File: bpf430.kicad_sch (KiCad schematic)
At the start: 39 parts

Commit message: 部品定数を入力　ただし未評価
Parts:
- C403, C405, C407, C409, C411, C413, C415, C417, C419, C421, C423, C425, C427: value 1p -> NM
- C404, C428: value 10p -> 12p
- C410, C426: value 10p -> 15p
- C418: value 10p -> 5p
- L403, L405: value 10n -> NM
- L404, L406: value 1u -> 3.3n
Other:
- note added: "1t D3.5mm L2.0mm"
- note added: "Butterworth 410M-460M 6.68p, 3.32p, 34.0p"
- company: (none) -> JK1MLY / PRUG
- title: (none) -> FM QRP TRCV

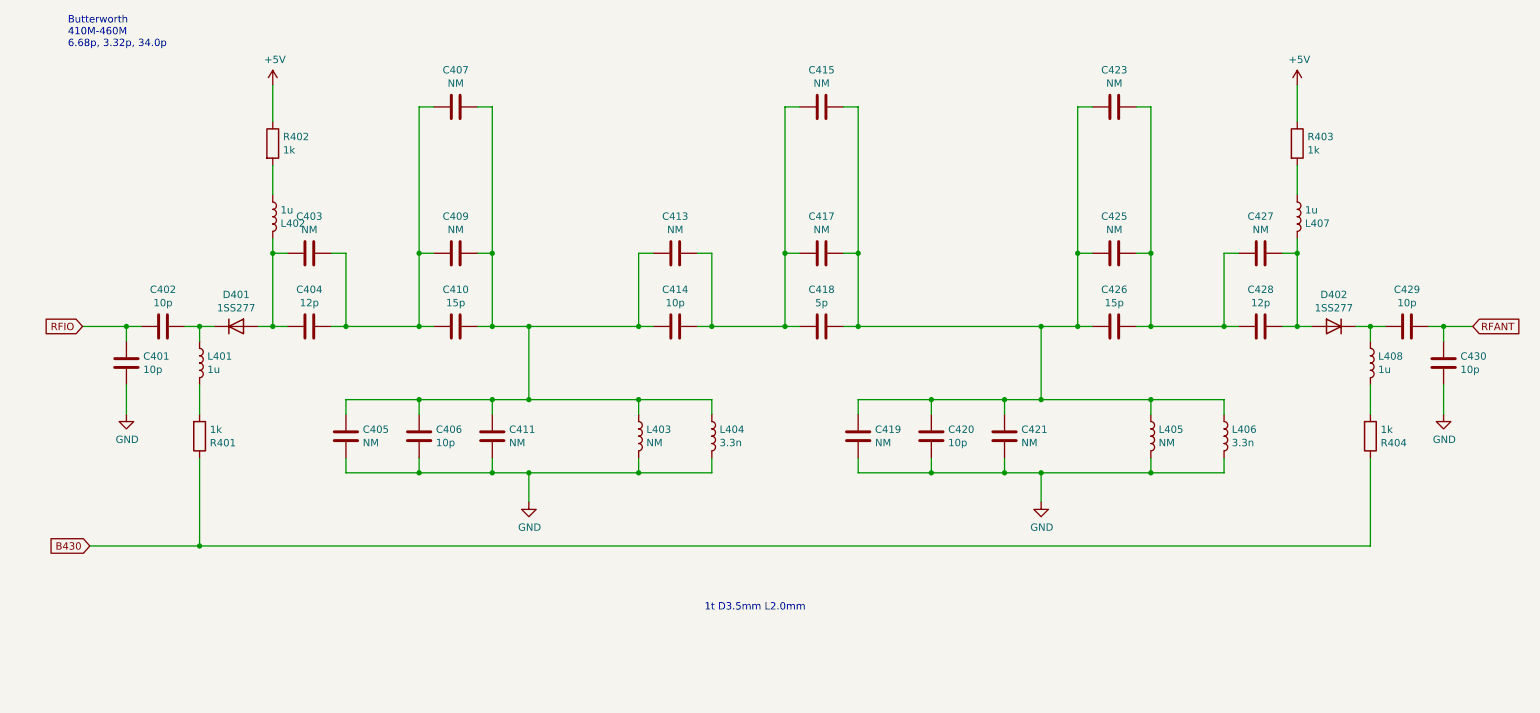
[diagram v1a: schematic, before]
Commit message: バンドパスフィルタの定数を見直し（単体試験の反映）
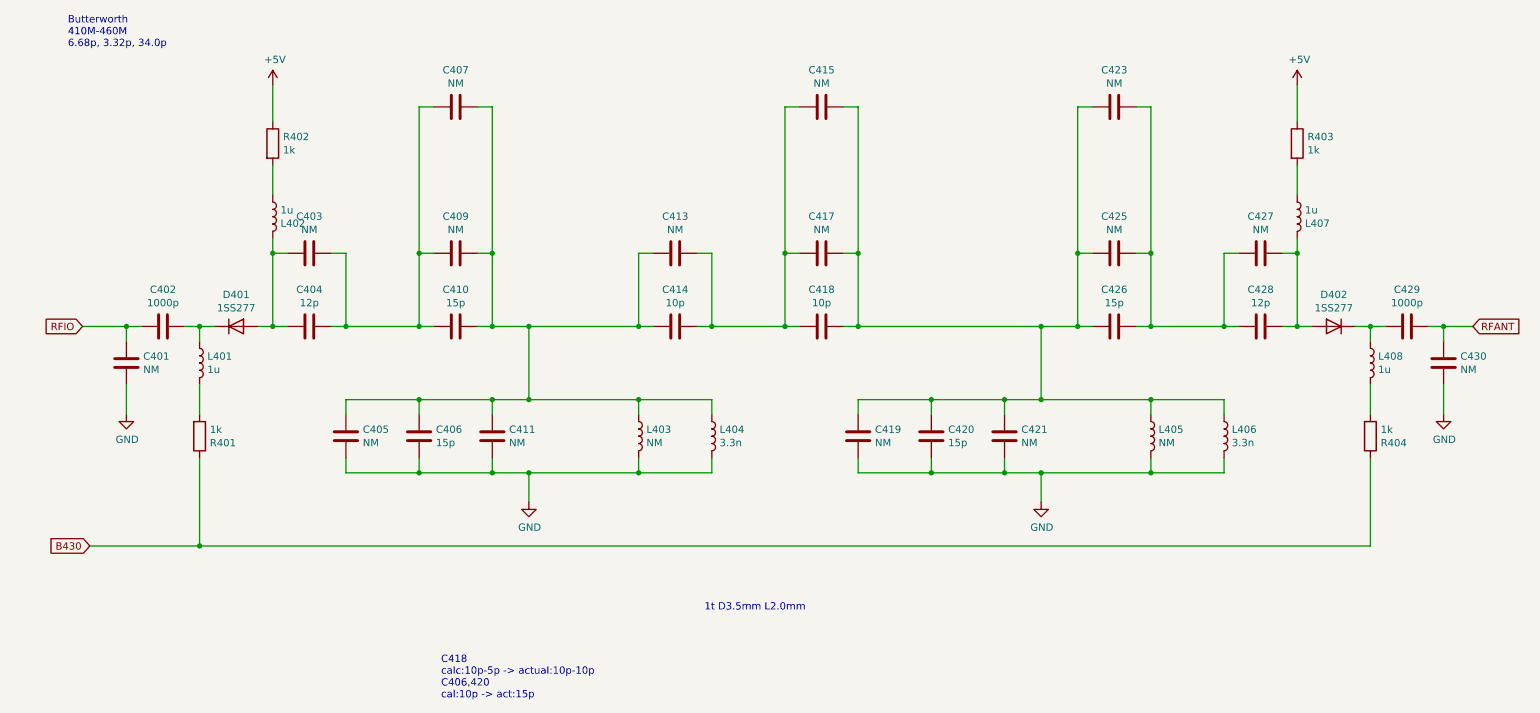
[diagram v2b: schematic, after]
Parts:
- C401, C430: value 10p -> NM
- C402, C429: value 10p -> 1000p
- C406, C420: value 10p -> 15p
- C418: value 5p -> 10p
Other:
- note added: "C418 calc:10p-5p -> actual:10p-10p C406,420 cal:10p -> act:15p"
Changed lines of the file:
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@@
+    (effects (font (size 1.27 1.27)) (justify left bottom))
+  )
+  (text "C418\ncalc:10p-5p -> actual:10p-10p\nC406,420\ncal:10p -> act:15p"
+    (at 92.71 140.97 0)
     (effects (font (size 1.27 1.27)) (justify left bottom))
   )
@@
       (effects (font (size 1.27 1.27)) (justify left))
     )
-    (property "Value" "10p" (id 1) (at 180.721 96.393 0)
+    (property "Value" "15p" (id 1) (at 180.721 96.393 0)
       (effects (font (size 1.27 1.27)) (justify left))
     )
@@
     (in_bom yes) (on_board yes)
     (property "Reference" "C418" (id 0) (at 158.75 69.7992 90))
-    (property "Value" "5p" (id 1) (at 158.75 72.1106 90))
+    (property "Value" "10p" (id 1) (at 158.75 72.1106 90))
     (property "Footprint" "Capacitor_THT:C_Disc_D3.4mm_W2.1mm_P2.50mm" (id 2) (at 162.56 75.2348 0)
       (effects (font (size 1.27 1.27)) hide)
@@
       (effects (font (size 1.27 1.27)) (justify left))
     )
-    (property "Value" "10p" (id 1) (at 91.821 96.393 0)
+    (property "Value" "15p" (id 1) (at 91.821 96.393 0)
       (effects (font (size 1.27 1.27)) (justify left))
     )
@@
     (in_bom yes) (on_board yes)
     (property "Reference" "C429" (id 0) (at 260.35 69.7992 90))
-    (property "Value" "10p" (id 1) (at 260.35 72.1106 90))
+    (property "Value" "1000p" (id 1) (at 260.35 72.1106 90))
     (property "Footprint" "Capacitor_THT:C_Disc_D3.4mm_W2.1mm_P2.50mm" (id 2) (at 264.16 75.2348 0)
       (effects (font (size 1.27 1.27)) hide)
@@
     (in_bom yes) (on_board yes)
     (property "Reference" "C402" (id 0) (at 44.45 69.7992 90))
-    (property "Value" "10p" (id 1) (at 44.45 72.1106 90))
+    (property "Value" "1000p" (id 1) (at 44.45 72.1106 90))
     (property "Footprint" "Capacitor_THT:C_Disc_D3.4mm_W2.1mm_P2.50mm" (id 2) (at 48.26 75.2348 0)
       (effects (font (size 1.27 1.27)) hide)
@@
       (effects (font (size 1.27 1.27)) (justify left))
     )
-    (property "Value" "10p" (id 1) (at 41.021 83.693 0)
+    (property "Value" "NM" (id 1) (at 41.021 83.693 0)
       (effects (font (size 1.27 1.27)) (justify left))
     )
@@
       (effects (font (size 1.27 1.27)) (justify left))
     )
-    (property "Value" "10p" (id 1) (at 269.621 83.693 0)
-      (effects (font (size 1.27 1.27)) (justify left))
-    )
+    (property "Value" "NM" (id 1) (at 269.621 83.693 0)
+      (effects (font (size 1.27 1.27)) (justify left))
+    )

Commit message: Add files via upload
フィルタ回路変更とジャンパクリーン
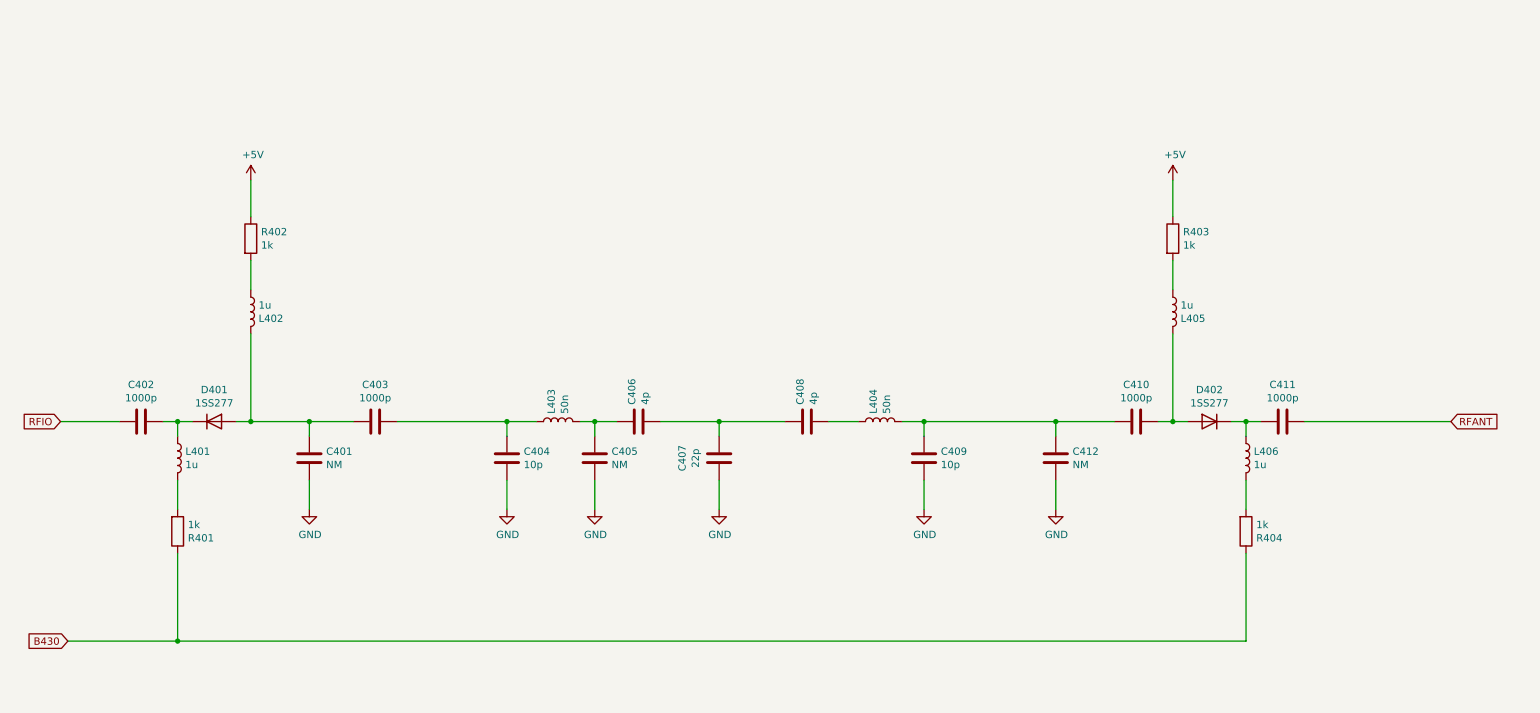
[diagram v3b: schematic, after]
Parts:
- removed C403, C411, C413, C415, C417, C419, C421, C423, C425, C427: NM, digikey-footprints:0603, symbol Device:C
- removed C410, C420, C426: 15p, Capacitor_THT:C_Disc_D3.4mm_W2.1mm_P2.50mm, symbol Device:C
- removed C414, C418: 10p, Capacitor_THT:C_Disc_D3.4mm_W2.1mm_P2.50mm, symbol Device:C
- removed L405: NM, Inductor_SMD:L_Murata_LQH2MCNxxxx02_2.0x1.6mm, symbol Device:L
- removed L406: 3.3n, Resistor_THT:R_Axial_DIN0204_L3.6mm_D1.6mm_P5.08mm_Horizontal, symbol Device:L
- added C404: 10p, Capacitor_THT:C_Disc_D3.4mm_W2.1mm_P2.50mm, symbol Device:C
- added C408: 4p, Capacitor_THT:C_Disc_D3.4mm_W2.1mm_P2.50mm, symbol Device:C
- C403: renamed from C404; value 12p -> 1000p
- C405: footprint digikey-footprints:0603 -> Capacitor_THT:C_Disc_D3.4mm_W2.1mm_P2.50mm
- C406: value 15p -> 4p
- C407: value NM -> 22p; footprint digikey-footprints:0603 -> Capacitor_THT:C_Disc_D3.4mm_W2.1mm_P2.50mm
- C409: value NM -> 10p; footprint digikey-footprints:0603 -> Capacitor_THT:C_Disc_D3.4mm_W2.1mm_P2.50mm
- C410: renamed from C428; value 12p -> 1000p
- L403: value NM -> 50n; footprint Inductor_SMD:L_Murata_LQH2MCNxxxx02_2.0x1.6mm -> usr-Library:coil3_7mm
- L404: value 3.3n -> 50n; footprint Resistor_THT:R_Axial_DIN0204_L3.6mm_D1.6mm_P5.08mm_Horizontal -> usr-Library:coil3_7mm
- renumbered C429 to C411, C430 to C412, L407 to L405, L408 to L406
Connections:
- net GND: now also C407.1, C409.2, C404.2; no longer C406.2, L403.2, L404.2
- net RFANT: no longer C412.1
- net RFIO: no longer C401.1
- net at C403.1, D401.2 (A), L402.1: now also C401.1
- net at C410.1: now also C409.1, C412.1, L404.2
- new net: C403.2, C404.1, L403.1
- new net: C405.1, C406.1, L403.2
- new net: C406.2, C407.2, C408.1
- new net: C408.2, L404.1
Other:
- note removed: "1t D3.5mm L2.0mm"
- note removed: "Butterworth 410M-460M 6.68p, 3.32p, 34.0p"
- note removed: "C418 calc:10p-5p -> actual:10p-10p C406,420 cal:10p -> act:15p"
- moved on the sheet: C401, C402, C403, C410, C411, C412, D401, D402, L401, L402, L405, L406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

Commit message: アップデート
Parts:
- removed C401, C412: NM, Capacitor_THT:C_Disc_D3.4mm_W2.1mm_P2.50mm, symbol Device:C
- removed C408: 4p, Capacitor_THT:C_Disc_D3.4mm_W2.1mm_P2.50mm, symbol Device:C
- added R102: 1k, Resistor_THT:R_Axial_DIN0207_L6.3mm_D2.5mm_P2.54mm_Vertical, symbol Device:R
- D401, D402: footprint Diode_THT:D_A-405_P2.54mm_Vertical_AnodeUp -> Diode_THT:D_T-1_P5.08mm_Horizontal
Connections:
- net +5V: now also R102.1
- net B430: now also R102.2
- net at C406.2, C407.2: now also L404.1
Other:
- note added: "15p"
- note added: "2p"
- note added: "NM"

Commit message: Add files via upload
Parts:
- C402, C403, C410, C411: value 1000p -> 0.01u
- C404, C409: value 10p -> 5p
- C405: value NM -> 3p
- C406: value 4p -> 15p
- C407: value 22p -> 3p
- L401, L402, L405, L406: value 1u -> 10u
- L403, L404: value 50n -> 20n
- R401, R402, R403, R404: value 1k -> 470
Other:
- note added: "L403,404は5mm 1.5T corecraft 164-01A06L相当 コアは抜き去る 以前はaitendoで入手できたが現在は不可"
- note removed: "15p"
- note removed: "2p"
- note removed: "NM"
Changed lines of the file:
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@@
   (title_block
     (title "FM QRP TRCV")
-    (date "2022-03-12")
+    (date "2023-08-12")
     (rev "1")
     (company "JK1MLY / PRUG")
@@
     (stroke (width 0) (type default))
   )
-  (text "2p" (at 144.78 104.14 0)
-    (effects (font (size 1.27 1.27)) (justify left bottom))
-  )
-  (text "15p" (at 124.46 82.55 0)
-    (effects (font (size 1.27 1.27)) (justify left bottom))
-  )
-  (text "NM" (at 180.34 104.14 0)
-    (effects (font (size 1.27 1.27)) (justify left bottom))
-  )
-  (text "2p" (at 123.19 104.14 0)
-    (effects (font (size 1.27 1.27)) (justify left bottom))
-  )
-  (text "NM" (at 107.95 104.14 0)
+  (text "L403,404は5mm 1.5T\ncorecraft 164-01A06L相当\nコアは抜き去る\n以前はaitendoで入手できたが現在は不可"
+    (at 114.3 73.66 0)
     (effects (font (size 1.27 1.27)) (justify left bottom))
   )
@@
       (effects (font (size 1.27 1.27)) (justify left))
     )
-    (property "Value" "1u" (at 233.7562 100.203 0)
+    (property "Value" "10u" (at 233.7562 100.203 0)
       (effects (font (size 1.27 1.27)) (justify left))
     )
@@
       (effects (font (size 1.27 1.27)) (justify left))
     )
-    (property "Value" "1k" (at 61.468 62.103 0)
+    (property "Value" "470" (at 61.468 62.103 0)
       (effects (font (size 1.27 1.27)) (justify left))
     )
@@
       (effects (font (size 1.27 1.27)) hide)
     )
-    (property "Datasheet" "~" (at 59.69 60.96 0)
+    (property "Datasheet" "R-25471" (at 59.69 60.96 0)
       (effects (font (size 1.27 1.27)) hide)
     )
@@
       (effects (font (size 1.27 1.27)) (justify left))
     )
-    (property "Value" "1k" (at 234.188 110.617 0)
+    (property "Value" "470" (at 234.188 110.617 0)
       (effects (font (size 1.27 1.27)) (justify left))
     )
@@
       (effects (font (size 1.27 1.27)) hide)
     )
-    (property "Datasheet" "~" (at 232.41 111.76 0)
+    (property "Datasheet" "R-25471" (at 232.41 111.76 0)
       (effects (font (size 1.27 1.27)) hide)
     )
@@
       (effects (font (size 1.27 1.27)))
     )
-    (property "Value" "1000p" (at 81.28 88.6206 90)
+    (property "Value" "0.01u" (at 81.28 88.6206 90)
       (effects (font (size 1.27 1.27)))
     )
@@
       (effects (font (size 1.27 1.27)) hide)
     )
-    (property "Datasheet" "~" (at 81.28 92.71 0)
+    (property "Datasheet" "sato" (at 81.28 92.71 0)
       (effects (font (size 1.27 1.27)) hide)
     )
@@
       (effects (font (size 1.27 1.27)))
     )
-    (property "Value" "1000p" (at 213.36 88.6206 90)
+    (property "Value" "0.01u" (at 213.36 88.6206 90)
       (effects (font (size 1.27 1.27)))
     )
@@
       (effects (font (size 1.27 1.27)) hide)
     )
-    (property "Datasheet" "~" (at 213.36 92.71 0)
+    (property "Datasheet" "sato" (at 213.36 92.71 0)
       (effects (font (size 1.27 1.27)) hide)
     )
@@
       (effects (font (size 1.27 1.27)) (justify left))
     )
-    (property "Value" "1u" (at 48.3362 100.203 0)
+    (property "Value" "10u" (at 48.3362 100.203 0)
       (effects (font (size 1.27 1.27)) (justify left))
     )
@@
       (effects (font (size 1.27 1.27)) (justify left))
     )
-    (property "Value" "1k" (at 48.768 110.617 0)
+    (property "Value" "470" (at 48.768 110.617 0)
       (effects (font (size 1.27 1.27)) (justify left))
     )
@@
       (effects (font (size 1.27 1.27)) hide)
     )
-    (property "Datasheet" "~" (at 46.99 111.76 0)
+    (property "Datasheet" "R-25471" (at 46.99 111.76 0)
       (effects (font (size 1.27 1.27)) hide)
     )
@@
       (effects (font (size 1.27 1.27)) (justify left))
     )
-    (property "Value" "1u" (at 61.0362 72.517 0)
+    (property "Value" "10u" (at 61.0362 72.517 0)
       (effects (font (size 1.27 1.27)) (justify left))
     )
@@
       (effects (font (size 1.27 1.27)) (justify left))
     )
-    (property "Value" "1k" (at 221.488 62.103 0)
+    (property "Value" "470" (at 221.488 62.103 0)
       (effects (font (size 1.27 1.27)) (justify left))
     )
@@
       (effects (font (size 1.27 1.27)) hide)
     )
-    (property "Datasheet" "~" (at 219.71 60.96 0)
+    (property "Datasheet" "R-25471" (at 219.71 60.96 0)
       (effects (font (size 1.27 1.27)) hide)
     )
@@
       (effects (font (size 1.27 1.27)) (justify left))
     )
-    (property "Value" "1u" (at 221.0562 72.517 0)
+    (property "Value" "10u" (at 221.0562 72.517 0)
       (effects (font (size 1.27 1.27)) (justify left))
     )
@@
       (effects (font (size 1.27 1.27)))
     )
-    (property "Value" "1000p" (at 238.76 88.6206 90)
+    (property "Value" "0.01u" (at 238.76 88.6206 90)
       (effects (font (size 1.27 1.27)))
     )
@@
       (effects (font (size 1.27 1.27)) hide)
     )
-    (property "Datasheet" "~" (at 238.76 92.71 0)
+    (property "Datasheet" "sato" (at 238.76 92.71 0)
       (effects (font (size 1.27 1.27)) hide)
     )
@@
       (effects (font (size 1.27 1.27)))
     )
-    (property "Value" "1000p" (at 40.64 88.6206 90)
+    (property "Value" "0.01u" (at 40.64 88.6206 90)
       (effects (font (size 1.27 1.27)))
     )
@@
       (effects (font (size 1.27 1.27)) hide)
     )
-    (property "Datasheet" "~" (at 40.64 92.71 0)
+    (property "Datasheet" "sato" (at 40.64 92.71 0)
       (effects (font (size 1.27 1.27)) hide)
     )
@@
       (effects (font (size 1.27 1.27)) (justify left))
     )
-    (property "Value" "NM" (at 122.301 100.203 0)
+    (property "Value" "3p" (at 122.301 100.203 0)
       (effects (font (size 1.27 1.27)) (justify left))
     )
@@
       (effects (font (size 1.27 1.27)) hide)
     )
-    (property "Datasheet" "~" (at 119.38 99.06 0)
+    (property "Datasheet" "sato" (at 119.38 99.06 0)
       (effects (font (size 1.27 1.27)) hide)
     )
@@
       (effects (font (size 1.27 1.27)) (justify left))
     )
-    (property "Value" "50n" (at 170.053 91.3638 0)
+    (property "Value" "20n" (at 170.053 91.3638 0)
       (effects (font (size 1.27 1.27)) (justify left))
     )
@@
       (effects (font (size 1.27 1.27)) hide)
     )
-    (property "Datasheet" "digikey 0805CS-3N3EJTS" (at 168.91 92.71 0)
+    (property "Datasheet" "aitendo" (at 168.91 92.71 0)
       (effects (font (size 1.27 1.27)) hide)
     )
@@
       (effects (font (size 1.27 1.27)) hide)
     )
-    (property "Datasheet" "~" (at 36.83 120.65 0)
+    (property "Datasheet" "R-25102" (at 36.83 120.65 0)
       (effects (font (size 1.27 1.27)) hide)
     )
@@
       (effects (font (size 1.27 1.27)) (justify left))
     )
-    (property "Value" "10p" (at 179.451 100.203 0)
+    (property "Value" "5p" (at 179.451 100.203 0)
       (effects (font (size 1.27 1.27)) (justify left))
     )
@@
       (effects (font (size 1.27 1.27)) hide)
     )
-    (property "Datasheet" "~" (at 176.53 99.06 0)
+    (property "Datasheet" "sato" (at 176.53 99.06 0)
       (effects (font (size 1.27 1.27)) hide)
     )
@@
       (effects (font (size 1.27 1.27)))
     )
-    (property "Value" "22p" (at 136.8806 99.06 90)
+    (property "Value" "3p" (at 136.8806 99.06 90)
       (effects (font (size 1.27 1.27)))
     )
@@
       (effects (font (size 1.27 1.27)) hide)
     )
-    (property "Datasheet" "~" (at 140.97 99.06 0)
+    (property "Datasheet" "sato" (at 140.97 99.06 0)
       (effects (font (size 1.27 1.27)) hide)
     )
@@
       (effects (font (size 1.27 1.27)) (justify left))
     )
-    (property "Value" "10p" (at 107.061 100.203 0)
+    (property "Value" "5p" (at 107.061 100.203 0)
       (effects (font (size 1.27 1.27)) (justify left))
     )
@@
       (effects (font (size 1.27 1.27)) hide)
     )
-    (property "Datasheet" "~" (at 104.14 99.06 0)
+    (property "Datasheet" "sato" (at 104.14 99.06 0)
       (effects (font (size 1.27 1.27)) hide)
     )
@@
       (effects (font (size 1.27 1.27)) (justify left))
     )
-    (property "Value" "4p" (at 128.143 89.789 0)
+    (property "Value" "15p" (at 128.143 89.789 0)
       (effects (font (size 1.27 1.27)) (justify left))
     )
@@
       (effects (font (size 1.27 1.27)) hide)
     )
-    (property "Datasheet" "~" (at 127 92.71 0)
+    (property "Datasheet" "sato" (at 127 92.71 0)
       (effects (font (size 1.27 1.27)) hide)
     )
@@
       (effects (font (size 1.27 1.27)) (justify left))
     )
-    (property "Value" "50n" (at 114.173 91.3638 0)
+    (property "Value" "20n" (at 114.173 91.3638 0)
       (effects (font (size 1.27 1.27)) (justify left))
     )
@@
       (effects (font (size 1.27 1.27)) hide)
     )
-    (property "Datasheet" "digikey 0805CS-3N3EJTS" (at 113.03 92.71 0)
-      (effects (font (size 1.27 1.27)) hide)
-    )
+    (property "Datasheet" "aitendo" (at 113.03 92.71 0)
+      (effects (font (size 1.27 1.27)) hide)
+    )
